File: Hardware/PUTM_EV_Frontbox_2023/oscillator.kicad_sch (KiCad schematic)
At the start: 3 parts, among them Y1 ABM8G-48.000MHZ

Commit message: Schematic ready for review
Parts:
- renumbered C11 to C23, C12 to C24
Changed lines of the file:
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@@
   (title_block
     (title "Oscillator")
-    (date "2023-02-24")
+    (date "2023-03-11")
     (rev "${REVISION}")
     (company "Author: Szymon Kostrubiec")
@@
   (symbol (lib_id "Device:C_Small") (at 147.32 97.79 0) (unit 1)
     (in_bom yes) (on_board yes) (dnp no)
-    (property "Reference" "C12" (at 149.86 97.79 0)
+    (property "Reference" "C24" (at 149.86 97.79 0)
       (effects (font (size 1.27 1.27)) (justify left))
     )
@@
       (project "PUTM_EV_Frontbox_2023"
         (path "/b652b05a-4e3d-4ad1-b032-18886abe7d45/4deadd9b-3e18-4284-beb5-6600402c5311"
-          (reference "C12") (unit 1)
+          (reference "C24") (unit 1)
         )
       )
@@
   (symbol (lib_id "power:GND") (at 142.24 101.6 0) (unit 1)
     (in_bom yes) (on_board yes) (dnp no) (fields_autoplaced)
-    (property "Reference" "#PWR034" (at 142.24 107.95 0)
+    (property "Reference" "#PWR069" (at 142.24 107.95 0)
       (effects (font (size 1.27 1.27)) hide)
     )
@@
       (project "PUTM_EV_Frontbox_2023"
         (path "/b652b05a-4e3d-4ad1-b032-18886abe7d45/4deadd9b-3e18-4284-beb5-6600402c5311"
-          (reference "#PWR034") (unit 1)
+          (reference "#PWR069") (unit 1)
         )
       )
@@
   (symbol (lib_id "Device:C_Small") (at 137.16 97.79 0) (unit 1)
     (in_bom yes) (on_board yes) (dnp no)
-    (property "Reference" "C11" (at 129.54 97.79 0)
+    (property "Reference" "C23" (at 129.54 97.79 0)
       (effects (font (size 1.27 1.27)) (justify left))
     )
@@
       (project "PUTM_EV_Frontbox_2023"
         (path "/b652b05a-4e3d-4ad1-b032-18886abe7d45/4deadd9b-3e18-4284-beb5-6600402c5311"
-          (reference "C11") (unit 1)
+          (reference "C23") (unit 1)
         )
       )
@@
   (symbol (lib_id "power:GND") (at 142.24 90.17 180) (unit 1)
     (in_bom yes) (on_board yes) (dnp no) (fields_autoplaced)
-    (property "Reference" "#PWR035" (at 142.24 83.82 0)
+    (property "Reference" "#PWR068" (at 142.24 83.82 0)
       (effects (font (size 1.27 1.27)) hide)
     )
@@
       (project "PUTM_EV_Frontbox_2023"
         (path "/b652b05a-4e3d-4ad1-b032-18886abe7d45/4deadd9b-3e18-4284-beb5-6600402c5311"
-          (reference "#PWR035") (unit 1)
+          (reference "#PWR068") (unit 1)
         )
       )

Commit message: Fixed all issues
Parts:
- Y1: symbol Device:Crystal_GND23_Small -> Device:Crystal_GND24_Small
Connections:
- net GND: now also Y1.4; no longer Y1.3
- net HSE_OUT: now also Y1.3; no longer Y1.4
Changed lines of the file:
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@@
     )
   )
-  (symbol (lib_id "Device:Crystal_GND23_Small") (at 142.24 93.98 0) (unit 1)
+  (symbol (lib_id "Device:Crystal_GND24_Small") (at 142.24 93.98 0) (unit 1)
     (in_bom yes) (on_board yes) (dnp no)
     (property "Reference" "Y1" (at 146.05 96.52 0)
@@
       (effects (font (size 1.27 1.27)) hide)
     )
-    (property "Datasheet" "https://www.mouser.pl/ProductDetail/ABRACON/ABM8G-48.000MHZ-B4Y-T?qs=3LVMET7lfiMdaGoXTgMQvQ%3D%3D" (at 142.24 93.98 0)
+    (property "Datasheet" "~" (at 142.24 93.98 0)
       (effects (font (size 1.27 1.27)) hide)
     )

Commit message: Schematic modified, footprints assigned
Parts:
- C23, C24: footprint (none) -> Capacitor_SMD:C_0402_1005Metric_Pad0.74x0.62mm_HandSolder
- Y1: footprint (none) -> Crystal:Crystal_SMD_Abracon_ABM8G-4Pin_3.2x2.5mm
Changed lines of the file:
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@@
       (effects (font (size 1.27 1.27)) (justify left))
     )
-    (property "Footprint" "" (at 147.32 97.79 0)
+    (property "Footprint" "Capacitor_SMD:C_0402_1005Metric_Pad0.74x0.62mm_HandSolder" (at 147.32 97.79 0)
       (effects (font (size 1.27 1.27)) hide)
     )
@@
       (effects (font (size 1.27 1.27)))
     )
-    (property "Footprint" "" (at 142.24 93.98 0)
+    (property "Footprint" "Crystal:Crystal_SMD_Abracon_ABM8G-4Pin_3.2x2.5mm" (at 142.24 93.98 0)
       (effects (font (size 1.27 1.27)) hide)
     )
-    (property "Datasheet" "~" (at 142.24 93.98 0)
+    (property "Datasheet" "https://www.mouser.pl/datasheet/2/3/ABM8G-1608872.pdf" (at 142.24 93.98 0)
       (effects (font (size 1.27 1.27)) hide)
     )
@@
       (effects (font (size 1.27 1.27)) (justify left))
     )
-    (property "Footprint" "" (at 137.16 97.79 0)
+    (property "Footprint" "Capacitor_SMD:C_0402_1005Metric_Pad0.74x0.62mm_HandSolder" (at 137.16 97.79 0)
       (effects (font (size 1.27 1.27)) hide)
     )

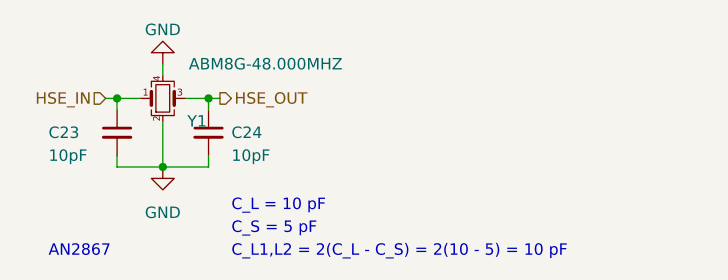
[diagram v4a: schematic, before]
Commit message: Added gearbox temperature sensors on schematic
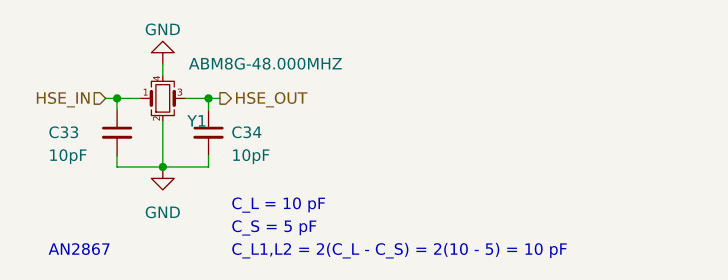
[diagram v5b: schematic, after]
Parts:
- renumbered C23 to C33, C24 to C34
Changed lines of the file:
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@@
   (symbol (lib_id "Device:C_Small") (at 147.32 97.79 0) (unit 1)
     (in_bom yes) (on_board yes) (dnp no)
-    (property "Reference" "C24" (at 149.86 97.79 0)
+    (property "Reference" "C34" (at 149.86 97.79 0)
       (effects (font (size 1.27 1.27)) (justify left))
     )
@@
       (project "PUTM_EV_Frontbox_2023"
         (path "/b652b05a-4e3d-4ad1-b032-18886abe7d45/4deadd9b-3e18-4284-beb5-6600402c5311"
-          (reference "C24") (unit 1)
+          (reference "C34") (unit 1)
         )
       )
@@
   (symbol (lib_id "power:GND") (at 142.24 101.6 0) (unit 1)
     (in_bom yes) (on_board yes) (dnp no) (fields_autoplaced)
-    (property "Reference" "#PWR069" (at 142.24 107.95 0)
+    (property "Reference" "#PWR078" (at 142.24 107.95 0)
       (effects (font (size 1.27 1.27)) hide)
     )
@@
       (project "PUTM_EV_Frontbox_2023"
         (path "/b652b05a-4e3d-4ad1-b032-18886abe7d45/4deadd9b-3e18-4284-beb5-6600402c5311"
-          (reference "#PWR069") (unit 1)
+          (reference "#PWR078") (unit 1)
         )
       )
@@
     (instances
       (project "PUTM_EV_Frontbox_2023"
-        (path "/b652b05a-4e3d-4ad1-b032-18886abe7d45"
-          (reference "Y1") (unit 1)
-        )
         (path "/b652b05a-4e3d-4ad1-b032-18886abe7d45/4deadd9b-3e18-4284-beb5-6600402c5311"
           (reference "Y1") (unit 1)
@@
   (symbol (lib_id "Device:C_Small") (at 137.16 97.79 0) (unit 1)
     (in_bom yes) (on_board yes) (dnp no)
-    (property "Reference" "C23" (at 129.54 97.79 0)
+    (property "Reference" "C33" (at 129.54 97.79 0)
       (effects (font (size 1.27 1.27)) (justify left))
     )
@@
       (project "PUTM_EV_Frontbox_2023"
         (path "/b652b05a-4e3d-4ad1-b032-18886abe7d45/4deadd9b-3e18-4284-beb5-6600402c5311"
-          (reference "C23") (unit 1)
+          (reference "C33") (unit 1)
         )
       )
@@
   (symbol (lib_id "power:GND") (at 142.24 90.17 180) (unit 1)
     (in_bom yes) (on_board yes) (dnp no) (fields_autoplaced)
-    (property "Reference" "#PWR068" (at 142.24 83.82 0)
+    (property "Reference" "#PWR077" (at 142.24 83.82 0)
       (effects (font (size 1.27 1.27)) hide)
     )
@@
       (project "PUTM_EV_Frontbox_2023"
         (path "/b652b05a-4e3d-4ad1-b032-18886abe7d45/4deadd9b-3e18-4284-beb5-6600402c5311"
-          (reference "#PWR068") (unit 1)
+          (reference "#PWR077") (unit 1)
         )
       )
